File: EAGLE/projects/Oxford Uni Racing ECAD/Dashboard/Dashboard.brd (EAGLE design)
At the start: 165.1 x 153.3 mm, 6 parts, among them J1 T821108A1S100CEU, J3 T821108A1S100CEU, K1 EC2-12NU, K2 EC2-12NU, X2 D-SUB9-H2M09ST

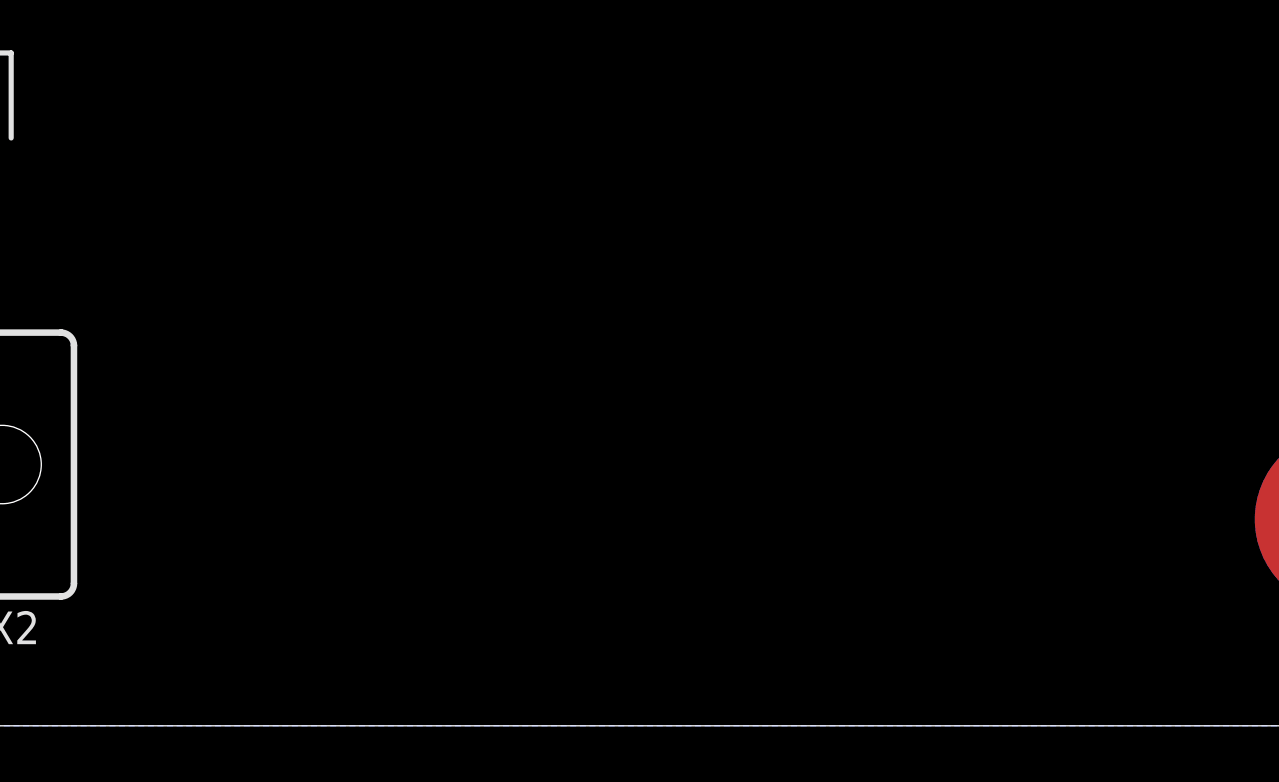
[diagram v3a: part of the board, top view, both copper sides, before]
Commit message: added power delivery to dashboard
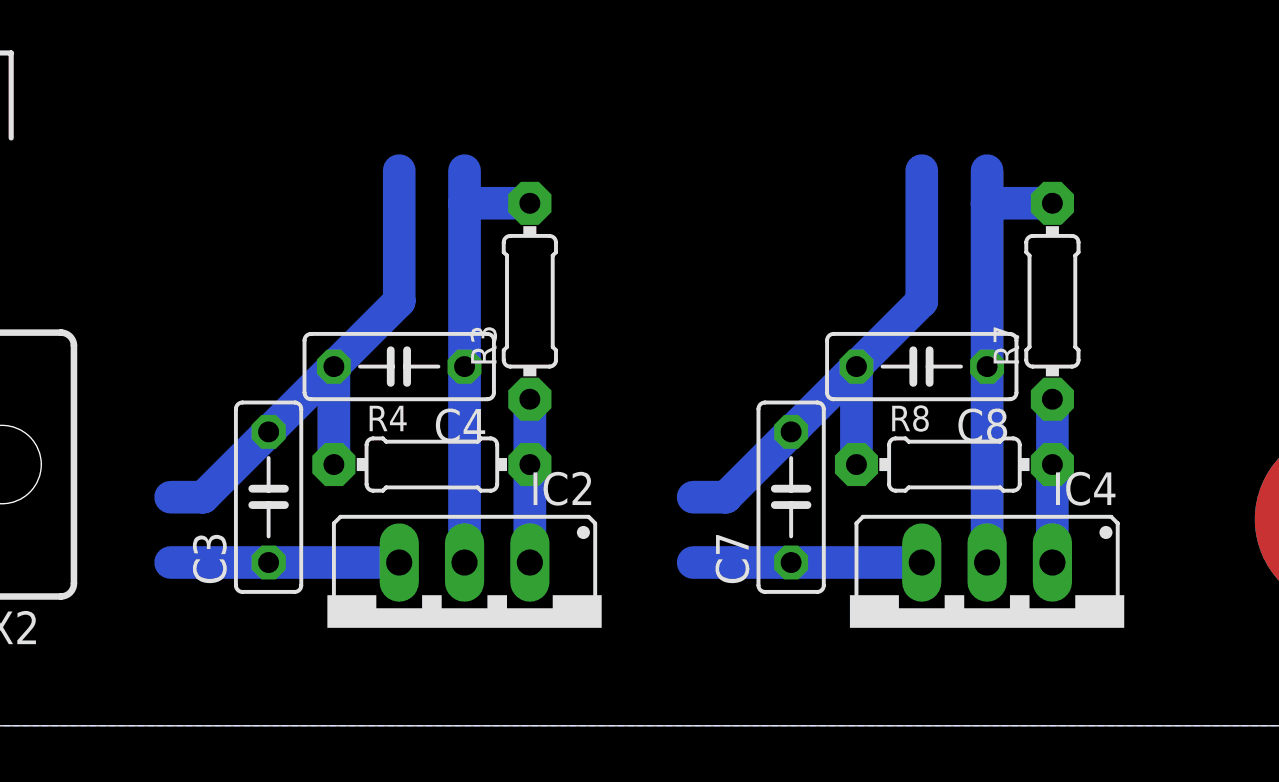
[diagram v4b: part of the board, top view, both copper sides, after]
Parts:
- added C3, C7: 0.1uF, adafruit:C050-025X075
- added C4, C8: 1uF, adafruit:C050-025X075
- added IC2, IC4: (no value), v-reg:317TS
- added R3, R7: 240, adafruit:0204/7
- added R4: 390, adafruit:0204/7
- added R8: 720, adafruit:0204/7
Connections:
- new net 3.3V: C4.1, IC2.2, R3.2
- new net N$2: IC2.1, R3.1, R4.2
- new net N$6: IC4.1, R7.1, R8.2
- net 12V: now also C3.1, C7.1, IC2.3, IC4.3
- net 5V: now also C8.1, IC4.2, R7.2
- net GND: now also C3.2, C4.2, C7.2, C8.2, R4.1, R8.1
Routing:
- net GND: track 76.8 -> 118.7 mm
- net 5V: track 0.00 -> 17.8 mm
- net 3.3V: track 0.00 -> 17.8 mm
- net 12V: track 25.2 -> 43.0 mm
- net N$6: track 0.00 -> 6.35 mm
- net N$2: track 0.00 -> 6.35 mm
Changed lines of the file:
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@@
 <attribute name="VALUE" x="100.33" y="25.4" size="1.27" layer="27" rot="R180" align="center"/>
+</element>
+<element name="IC2" library="v-reg" library_urn="urn:adsk.eagle:library:409" package="317TS" package3d_urn="urn:adsk.eagle:package:30353/1" value="" x="123.19" y="3.81" smashed="yes" rot="R180">
+<attribute name="NAME" x="128.27" y="9.8552" size="1.27" layer="25" ratio="10" rot="R180"/>
+<attribute name="VALUE" x="128.27" y="11.43" size="1.27" layer="27" ratio="10" rot="R180"/>
+</element>
+<element name="R3" library="adafruit" library_urn="urn:adsk.eagle:library:420" package="0204/7" package3d_urn="urn:adsk.eagle:package:6240596/1" value="240" x="125.73" y="16.51" smashed="yes" rot="R90">
+<attribute name="NAME" x="124.4346" y="13.97" size="0.9906" layer="25" ratio="12" rot="R90"/>
+<attribute name="VALUE" x="126.2126" y="14.8844" size="0.9906" layer="27" ratio="12" rot="R90"/>
+</element>
+<element name="R4" library="adafruit" library_urn="urn:adsk.eagle:library:420" package="0204/7" package3d_urn="urn:adsk.eagle:package:6240596/1" value="390" x="121.92" y="10.16" smashed="yes">
+<attribute name="NAME" x="119.38" y="11.4554" size="0.9906" layer="25" ratio="12"/>
+<attribute name="VALUE" x="120.2944" y="9.6774" size="0.9906" layer="27" ratio="12"/>
+</element>
+<element name="C3" library="adafruit" library_urn="urn:adsk.eagle:library:420" package="C050-025X075" package3d_urn="urn:adsk.eagle:package:6240357/1" value="0.1uF" x="115.57" y="8.89" smashed="yes" rot="R90">
+<attribute name="NAME" x="113.919" y="5.461" size="1.27" layer="25" ratio="10" rot="R90"/>
+<attribute name="VALUE" x="118.364" y="5.461" size="1.27" layer="27" ratio="10" rot="R90"/>
+</element>
+<element name="C4" library="adafruit" library_urn="urn:adsk.eagle:library:420" package="C050-025X075" package3d_urn="urn:adsk.eagle:package:6240357/1" value="1uF" x="120.65" y="13.97" smashed="yes" rot="R180">
+<attribute name="NAME" x="124.079" y="12.319" size="1.27" layer="25" ratio="10" rot="R180"/>
+<attribute name="VALUE" x="124.079" y="16.764" size="1.27" layer="27" ratio="10" rot="R180"/>
+</element>
+<element name="IC4" library="v-reg" library_urn="urn:adsk.eagle:library:409" package="317TS" package3d_urn="urn:adsk.eagle:package:30353/1" value="" x="143.51" y="3.81" smashed="yes" rot="R180">
+<attribute name="NAME" x="148.59" y="9.8552" size="1.27" layer="25" ratio="10" rot="R180"/>
+<attribute name="VALUE" x="148.59" y="11.43" size="1.27" layer="27" ratio="10" rot="R180"/>
+</element>
+<element name="R7" library="adafruit" library_urn="urn:adsk.eagle:library:420" package="0204/7" package3d_urn="urn:adsk.eagle:package:6240596/1" value="240" x="146.05" y="16.51" smashed="yes" rot="R90">
+<attribute name="NAME" x="144.7546" y="13.97" size="0.9906" layer="25" ratio="12" rot="R90"/>
+<attribute name="VALUE" x="146.5326" y="14.8844" size="0.9906" layer="27" ratio="12" rot="R90"/>
+</element>
+<element name="R8" library="adafruit" library_urn="urn:adsk.eagle:library:420" package="0204/7" package3d_urn="urn:adsk.eagle:package:6240596/1" value="720" x="142.24" y="10.16" smashed="yes">
+<attribute name="NAME" x="139.7" y="11.4554" size="0.9906" layer="25" ratio="12"/>
+<attribute name="VALUE" x="140.6144" y="9.6774" size="0.9906" layer="27" ratio="12"/>
+</element>
+<element name="C7" library="adafruit" library_urn="urn:adsk.eagle:library:420" package="C050-025X075" package3d_urn="urn:adsk.eagle:package:6240357/1" value="0.1uF" x="135.89" y="8.89" smashed="yes" rot="R90">
+<attribute name="NAME" x="134.239" y="5.461" size="1.27" layer="25" ratio="10" rot="R90"/>
+<attribute name="VALUE" x="138.684" y="5.461" size="1.27" layer="27" ratio="10" rot="R90"/>
+</element>
+<element name="C8" library="adafruit" library_urn="urn:adsk.eagle:library:420" package="C050-025X075" package3d_urn="urn:adsk.eagle:package:6240357/1" value="1uF" x="140.97" y="13.97" smashed="yes" rot="R180">
+<attribute name="NAME" x="144.399" y="12.319" size="1.27" layer="25" ratio="10" rot="R180"/>
+<attribute name="VALUE" x="144.399" y="16.764" size="1.27" layer="27" ratio="10" rot="R180"/>
 </element>
 </elements>
@@
 <wire x1="97.79" y1="12.7" x2="97.79" y2="20.32" width="1.27" layer="16"/>
 <wire x1="97.79" y1="20.32" x2="97.79" y2="22.86" width="1.27" layer="16"/>
+<contactref element="C3" pad="2"/>
+<contactref element="R4" pad="1"/>
+<contactref element="C4" pad="2"/>
+<wire x1="115.57" y1="11.43" x2="113.03" y2="8.89" width="1.27" layer="16"/>
+<wire x1="113.03" y1="8.89" x2="111.76" y2="8.89" width="1.27" layer="16"/>
+<wire x1="115.57" y1="11.43" x2="118.11" y2="13.97" width="1.27" layer="16"/>
+<wire x1="118.11" y1="10.16" x2="118.11" y2="13.97" width="1.27" layer="16"/>
+<wire x1="118.11" y1="13.97" x2="120.65" y2="16.51" width="1.27" layer="16"/>
+<wire x1="120.65" y1="16.51" x2="120.65" y2="21.59" width="1.27" layer="16"/>
+<contactref element="C7" pad="2"/>
+<contactref element="R8" pad="1"/>
+<contactref element="C8" pad="2"/>
+<wire x1="135.89" y1="11.43" x2="133.35" y2="8.89" width="1.27" layer="16"/>
+<wire x1="133.35" y1="8.89" x2="132.08" y2="8.89" width="1.27" layer="16"/>
+<wire x1="135.89" y1="11.43" x2="138.43" y2="13.97" width="1.27" layer="16"/>
+<wire x1="138.43" y1="10.16" x2="138.43" y2="13.97" width="1.27" layer="16"/>
+<wire x1="138.43" y1="13.97" x2="140.97" y2="16.51" width="1.27" layer="16"/>
+<wire x1="140.97" y1="16.51" x2="140.97" y2="21.59" width="1.27" layer="16"/>
+<wire x1="120.65" y1="16.51" x2="132.08" y2="8.89" width="0" layer="19" extent="16-16"/>
+<wire x1="101.6" y1="11.43" x2="111.76" y2="8.89" width="0" layer="19" extent="16-16"/>
 <wire x1="20.32" y1="-4.86" x2="92.71" y2="8.7376" width="0" layer="19" extent="1-1"/>
 </signal>
@@
 <contactref element="J3" pad="2"/>
 <wire x1="100.33" y1="20.32" x2="100.33" y2="22.86" width="1.27" layer="16"/>
+<contactref element="IC2" pad="3"/>
+<contactref element="C3" pad="1"/>
+<wire x1="120.65" y1="6.35" x2="115.57" y2="6.35" width="1.27" layer="16"/>
+<wire x1="115.57" y1="6.35" x2="111.76" y2="6.35" width="1.27" layer="16"/>
+<contactref element="IC4" pad="3"/>
+<contactref element="C7" pad="1"/>
+<wire x1="140.97" y1="6.35" x2="135.89" y2="6.35" width="1.27" layer="16"/>
+<wire x1="135.89" y1="6.35" x2="132.08" y2="6.35" width="1.27" layer="16"/>
+<wire x1="120.65" y1="6.35" x2="132.08" y2="6.35" width="0" layer="19" extent="16-16"/>
+<wire x1="100.33" y1="20.32" x2="111.76" y2="6.35" width="0" layer="19" extent="16-16"/>
 <wire x1="3.81" y1="-12.92" x2="100.33" y2="20.32" width="0" layer="19" extent="1-1"/>
 </signal>
@@
 <signal name="5V">
 <contactref element="X2" pad="9"/>
+<contactref element="IC4" pad="2"/>
+<contactref element="C8" pad="1"/>
+<contactref element="R7" pad="2"/>
+<wire x1="143.51" y1="6.35" x2="143.51" y2="13.97" width="1.27" layer="16"/>
+<wire x1="143.51" y1="13.97" x2="143.51" y2="20.32" width="1.27" layer="16"/>
+<wire x1="143.51" y1="20.32" x2="143.51" y2="21.59" width="1.27" layer="16"/>
+<wire x1="146.05" y1="20.32" x2="143.51" y2="20.32" width="1.27" layer="16"/>
+<wire x1="88.5571" y1="11.5824" x2="143.51" y2="13.97" width="0" layer="19" extent="1-1"/>
+</signal>
+<signal name="N$2">
+<contactref element="IC2" pad="1"/>
+<contactref element="R4" pad="2"/>
+<contactref element="R3" pad="1"/>
+<wire x1="125.73" y1="6.35" x2="125.73" y2="10.16" width="1.27" layer="16"/>
+<wire x1="125.73" y1="12.7" x2="125.73" y2="10.16" width="1.27" layer="16"/>
+</signal>
+<signal name="3.3V">
+<contactref element="IC2" pad="2"/>
+<contactref element="C4" pad="1"/>
+<contactref element="R3" pad="2"/>
+<wire x1="123.19" y1="6.35" x2="123.19" y2="13.97" width="1.27" layer="16"/>
+<wire x1="123.19" y1="13.97" x2="123.19" y2="20.32" width="1.27" layer="16"/>
+<wire x1="123.19" y1="20.32" x2="123.19" y2="21.59" width="1.27" layer="16"/>
+<wire x1="125.73" y1="20.32" x2="123.19" y2="20.32" width="1.27" layer="16"/>
+</signal>
+<signal name="N$6">
+<contactref element="IC4" pad="1"/>
+<contactref element="R8" pad="2"/>
+<contactref element="R7" pad="1"/>
+<wire x1="146.05" y1="6.35" x2="146.05" y2="10.16" width="1.27" layer="16"/>
+<wire x1="146.05" y1="12.7" x2="146.05" y2="10.16" width="1.27" layer="16"/>
 </signal>
 </signals>

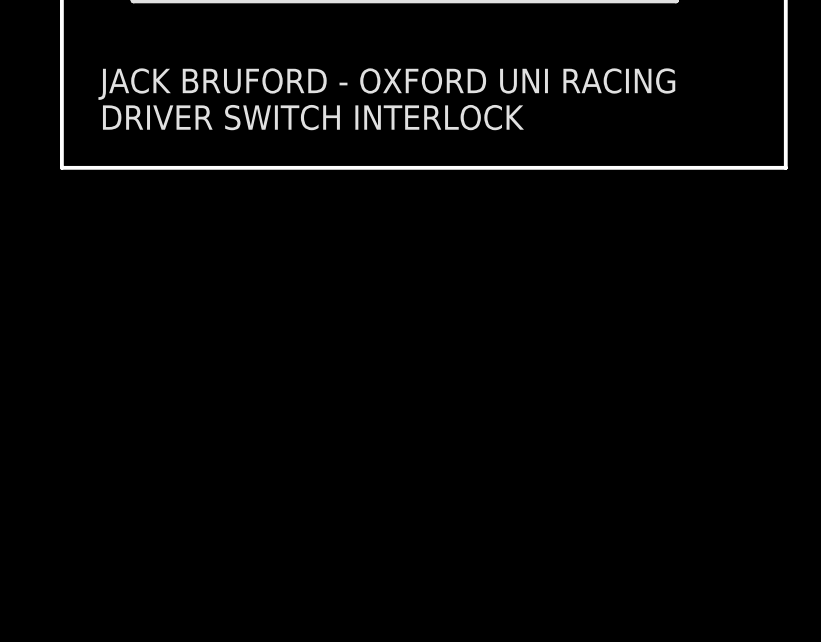
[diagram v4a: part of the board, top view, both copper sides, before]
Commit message: added CAN OUT to dashboard
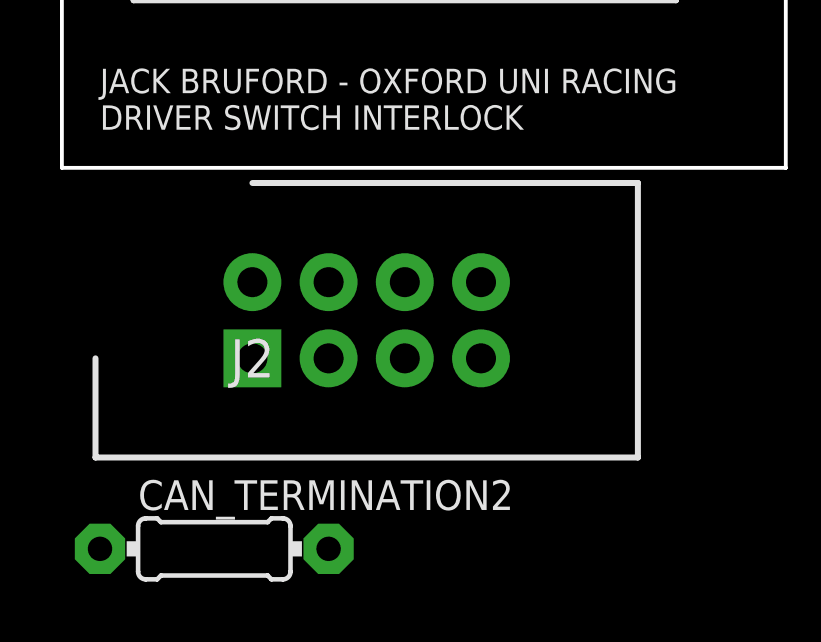
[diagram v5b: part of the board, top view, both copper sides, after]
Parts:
- added CAN_TERMINATION2: 120, adafruit:0204/7
- added J2: CAN_OUT, T821108A1S100CEU:HDRV8W64P254_2X4_1778X895X915P
- J3: value T821108A1S100CEU -> PWR_CAN
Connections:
- net 5V: now also J2.1, J2.2
- net CANH: now also CAN_TERMINATION2.2, J2.7, J2.8
- net CANL: now also CAN_TERMINATION2.1, J2.5, J2.6
- net GND: now also J2.3, J2.4
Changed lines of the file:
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@@
 <attribute name="VALUE" x="93.0656" y="29.6926" size="0.9906" layer="27" ratio="12" rot="R180"/>
 </element>
-<element name="J3" library="T821108A1S100CEU" package="HDRV8W64P254_2X4_1778X895X915P" value="T821108A1S100CEU" x="100.33" y="22.86" smashed="yes" rot="R180">
+<element name="J3" library="T821108A1S100CEU" package="HDRV8W64P254_2X4_1778X895X915P" value="PWR_CAN" x="100.33" y="22.86" smashed="yes" rot="R180">
 <attribute name="DESCRIPTION" value="HEADER, VERTICAL, 2.54MM, 8WAY Amphenol T821 Series, 2.54mm Pitch 8 Way 2 Row Straight PCB Header, Solder Termination, 3A" x="104.14" y="22.86" size="1.778" layer="27" rot="R180" display="off"/>
 <attribute name="HEIGHT" value="9.15mm" x="104.14" y="22.86" size="1.778" layer="27" rot="R180" display="off"/>
@@
 <attribute name="NAME" x="144.399" y="12.319" size="1.27" layer="25" ratio="10" rot="R180"/>
 <attribute name="VALUE" x="144.399" y="16.764" size="1.27" layer="27" ratio="10" rot="R180"/>
+</element>
+<element name="CAN_TERMINATION2" library="adafruit" library_urn="urn:adsk.eagle:library:420" package="0204/7" package3d_urn="urn:adsk.eagle:package:6240596/1" value="120" x="5.08" y="-52.07" smashed="yes">
+<attribute name="NAME" x="2.54" y="-50.7746" size="0.9906" layer="25" ratio="12"/>
+<attribute name="VALUE" x="3.4544" y="-52.5526" size="0.9906" layer="27" ratio="12"/>
+</element>
+<element name="J2" library="T821108A1S100CEU" package="HDRV8W64P254_2X4_1778X895X915P" value="CAN_OUT" x="6.35" y="-45.72" smashed="yes">
+<attribute name="DESCRIPTION" value="HEADER, VERTICAL, 2.54MM, 8WAY Amphenol T821 Series, 2.54mm Pitch 8 Way 2 Row Straight PCB Header, Solder Termination, 3A" x="6.35" y="-50.8" size="1.778" layer="27" display="off"/>
+<attribute name="HEIGHT" value="9.15mm" x="6.35" y="-50.8" size="1.778" layer="27" display="off"/>
+<attribute name="MANUFACTURER_NAME" value="Amphenol" x="6.35" y="-50.8" size="1.778" layer="27" display="off"/>
+<attribute name="MANUFACTURER_PART_NUMBER" value="T821108A1S100CEU" x="6.35" y="-50.8" size="1.778" layer="27" display="off"/>
+<attribute name="NAME" x="6.35" y="-45.72" size="1.27" layer="25" align="center"/>
+<attribute name="RS_PART_NUMBER" value="1702738" x="6.35" y="-50.8" size="1.778" layer="27" display="off"/>
+<attribute name="VALUE" x="6.35" y="-45.72" size="1.27" layer="27" align="center"/>
 </element>
 </elements>
@@
 <wire x1="138.43" y1="13.97" x2="140.97" y2="16.51" width="1.27" layer="16"/>
 <wire x1="140.97" y1="16.51" x2="140.97" y2="21.59" width="1.27" layer="16"/>
+<contactref element="J2" pad="4"/>
+<contactref element="J2" pad="3"/>
 <wire x1="120.65" y1="16.51" x2="132.08" y2="8.89" width="0" layer="19" extent="16-16"/>
 <wire x1="101.6" y1="11.43" x2="111.76" y2="8.89" width="0" layer="19" extent="16-16"/>
 <wire x1="20.32" y1="-4.86" x2="92.71" y2="8.7376" width="0" layer="19" extent="1-1"/>
+<wire x1="8.89" y1="-43.18" x2="7.62" y2="-27.94" width="0" layer="19" extent="1-1"/>
+<wire x1="8.89" y1="-45.72" x2="8.89" y2="-43.18" width="0" layer="19" extent="1-1"/>
 </signal>
 <signal name="DRIVERSWITCH-">
@@
 <wire x1="95.4786" y1="8.7376" x2="95.37065" y2="8.84555" width="0.6096" layer="16"/>
 <wire x1="95.37065" y1="8.84555" x2="95.37065" y2="13.97" width="0.6096" layer="16"/>
+<contactref element="CAN_TERMINATION2" pad="1"/>
+<contactref element="J2" pad="5"/>
+<contactref element="J2" pad="6"/>
 <wire x1="95.25" y1="20.32" x2="95.25" y2="22.86" width="0" layer="19" extent="1-1"/>
+<wire x1="11.43" y1="-43.18" x2="95.37065" y2="8.84555" width="0" layer="19" extent="16-16"/>
+<wire x1="11.43" y1="-45.72" x2="11.43" y2="-43.18" width="0" layer="19" extent="1-1"/>
+<wire x1="1.27" y1="-52.07" x2="11.43" y2="-45.72" width="0" layer="19" extent="1-1"/>
 </signal>
 <signal name="CANH">
@@
 <wire x1="92.71" y1="22.86" x2="87.63" y2="27.94" width="1.27" layer="16"/>
 <wire x1="87.63" y1="27.94" x2="87.63" y2="29.21" width="1.27" layer="16"/>
+<contactref element="CAN_TERMINATION2" pad="2"/>
+<contactref element="J2" pad="7"/>
+<contactref element="J2" pad="8"/>
+<wire x1="13.97" y1="-43.18" x2="92.71" y2="12.9667" width="0" layer="19" extent="16-16"/>
+<wire x1="13.97" y1="-45.72" x2="13.97" y2="-43.18" width="0" layer="19" extent="1-1"/>
+<wire x1="8.89" y1="-52.07" x2="13.97" y2="-45.72" width="0" layer="19" extent="1-1"/>
 </signal>
 <signal name="5V">
@@
 <wire x1="143.51" y1="20.32" x2="143.51" y2="21.59" width="1.27" layer="16"/>
 <wire x1="146.05" y1="20.32" x2="143.51" y2="20.32" width="1.27" layer="16"/>
+<contactref element="J2" pad="1"/>
+<contactref element="J2" pad="2"/>
 <wire x1="88.5571" y1="11.5824" x2="143.51" y2="13.97" width="0" layer="19" extent="1-1"/>
+<wire x1="6.35" y1="-43.18" x2="88.5571" y2="11.5824" width="0" layer="19" extent="1-1"/>
+<wire x1="6.35" y1="-45.72" x2="6.35" y2="-43.18" width="0" layer="19" extent="1-1"/>
 </signal>
 <signal name="N$2">
